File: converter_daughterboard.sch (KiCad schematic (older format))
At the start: 22 parts, among them P1 IN+, P2 IN GND, P3 OUT+, P4 OUT GND, P5 PC, P6 PR, P7 SC, U1 V28C, U2 DAUGHTERBOARD_MOUNT

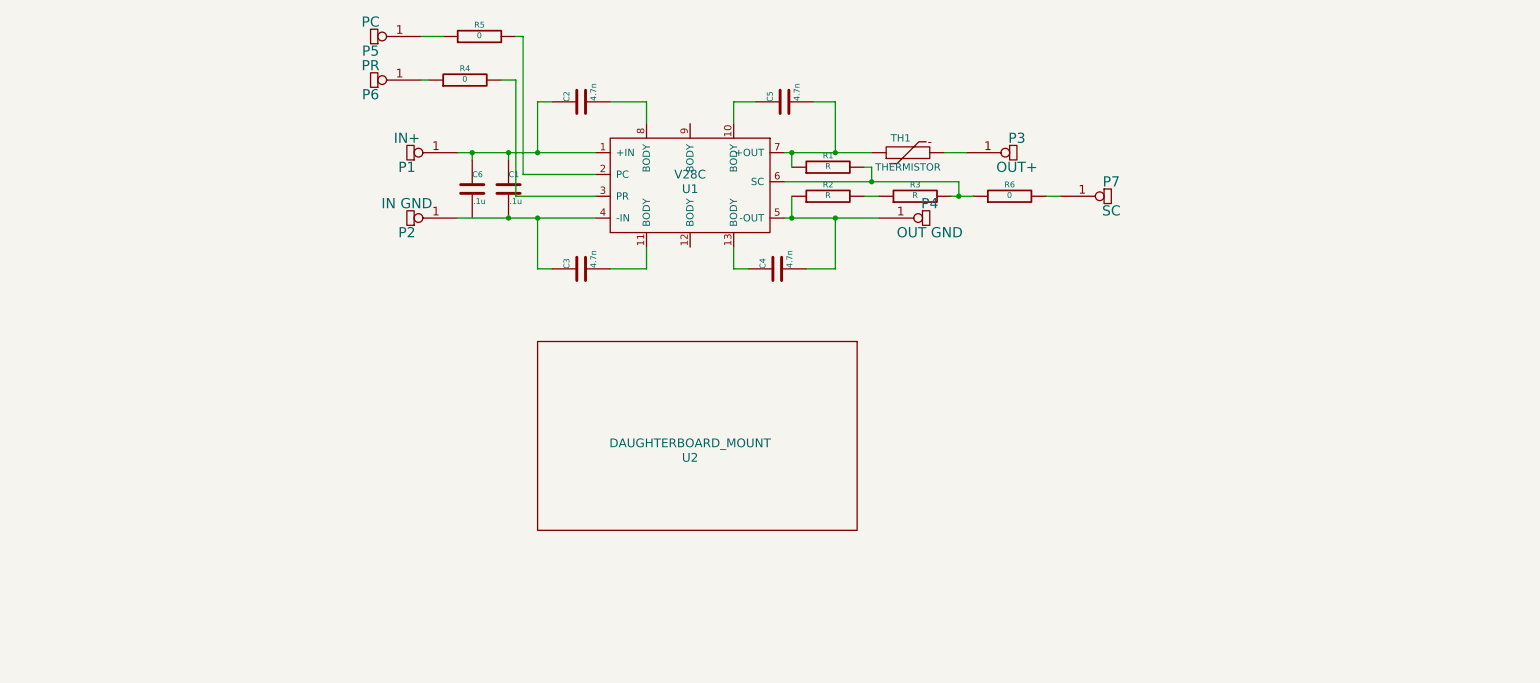
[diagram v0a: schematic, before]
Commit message: updating converter daughterboard for compatibility with DAC trimming for use with DCMG
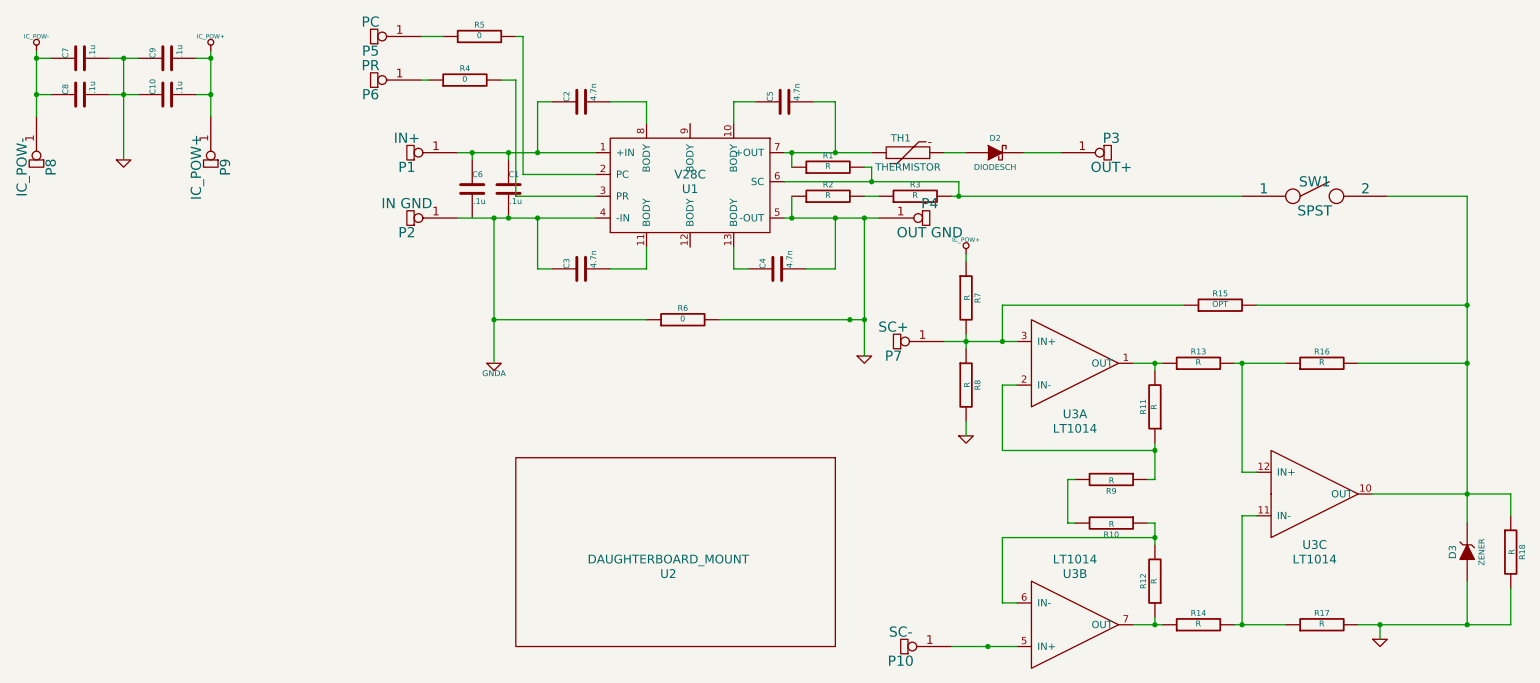
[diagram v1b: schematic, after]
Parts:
- added C10, C7, C8, C9: .1u, ~, symbol C
- added D2: DIODESCH, ~, symbol DIODESCH
- added D3: ZENER, ~, symbol ZENER
- added P10: SC-, ~, symbol CONNECTOR
- added P8: IC_POW-, ~, symbol CONNECTOR
- added P9: IC_POW+, ~, symbol CONNECTOR
- added R10, R11, R12, R13, R14, R16, R17, R18, R7, R8, R9: R, ~, symbol R
- added R15: OPT, ~, symbol R
- added SW1: SPST, ~, symbol SPST
- added U3: LT1014, ~, symbol LT1014
- P7: value SC -> SC+
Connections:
- net at P3.1 (W): now also D2.2 (K); no longer TH1.2
- net GND: now reaches C4.2, P4.1 (W), R2.1, U1.5 (-OUT)
- net GND: now also R6.2, C10.1, C7.2, C8.2, C9.1, D3.1 (A), R17.2, R18.2, R8.2
- net GNDA: now reaches C1.2, C3.1, P2.1 (W), U1.4 (-IN)
- net GNDA: now also R6.1
- net at R1.2, R3.2, U1.6 (SC): now also SW1.1; no longer R6.1
- net at P7.1 (W): now also R15.1, R7.2, R8.1, U3.3 (IN+); no longer R6.2
- new net: D2.1 (A), TH1.2
- new net: R11.2, R13.1, U3.1 (OUT)
- new net: R11.1, R9.1, U3.2 (IN-)
- new net: P10.1 (W), U3.5 (IN+)
- new net: R10.1, R12.2, U3.6 (IN-)
- new net: R12.1, R14.1, U3.7 (OUT)
- new net: D3.2 (K), R15.2, R16.2, R18.1, SW1.2, U3.10 (OUT)
- new net: R14.2, R17.1, U3.11 (IN-)
- new net: R13.2, R16.1, U3.12 (IN+)
- new net: R10.2, R9.2
- new net +12VA: U3.4 (+12VA), U3.4 (+12VA), U3.4 (+12VA)
- new net -12VA: U3.13 (-12VA), U3.13 (-12VA), U3.13 (-12VA)
- new net IC_POW+: C10.2, C9.2, P9.1 (W), R7.1
- new net IC_POW-: C7.1, C8.1, P8.1 (W)
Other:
- moved on the sheet: P3, P7, U2
